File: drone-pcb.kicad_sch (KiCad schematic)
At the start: 46 parts, among them J1 Conn_01x02_Pin, J10 Conn_01x03_Pin, J11 Conn_01x03_Pin, J12 Conn_01x03_Pin, J2 Conn_01x02_Pin, J3 Conn_01x02_Pin, J4 Conn_01x02_Pin, J5 Conn_01x02_Pin, J6 Conn_01x02_Pin, J7 USB_C_Receptacle_USB2.0_16P, J8 Conn_01x02_Pin, J9 Conn_01x03_Pin, Q1 AO3400A, Q2 AO3400A, Q3 AO3400A, Q4 AO3400A, Q5 AO3400A, Q6 AO3400A, SW1 CK_KMS2xxGP, U1 STM32F030C8Tx, U2 nRF24L01P, U3 MCP73831-2-OT, U4 TLV75533PDBV

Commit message: test export after makefile genaralisation
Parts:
- added U5: MPU-6050, Sensor_Motion:InvenSense_QFN-24_4x4mm_P0.5mm, symbol Sensor_Motion:MPU-6050
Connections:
- net battery+ is gone; now on net Vmotor: J8.1 (Pin_1), U3.3 (V_{BAT}), U4.1 (IN), U4.3 (EN)
- net +3V3: now also U5.13 (VDD)
- net GND: now also U5.18 (GND)
- net m1: no longer R11.1
- net m2: no longer R12.1
- net m3: no longer R13.1
- net m4: no longer R14.1
- net m5: no longer R15.1
- net m6: no longer R16.1
- net at Q1.1 (G), R1.1: now also R11.1
- net at Q3.1 (G), R3.1: now also R13.1
- net at Q2.1 (G), R2.1: now also R12.1
- net at Q4.1 (G), R4.1: now also R14.1
- net at Q5.1 (G), R5.1: now also R15.1
- net at Q6.1 (G), R6.1: now also R16.1
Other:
- note added: "3.3V power rail buck from battery voltage"
- note removed: "3.3V power rail"

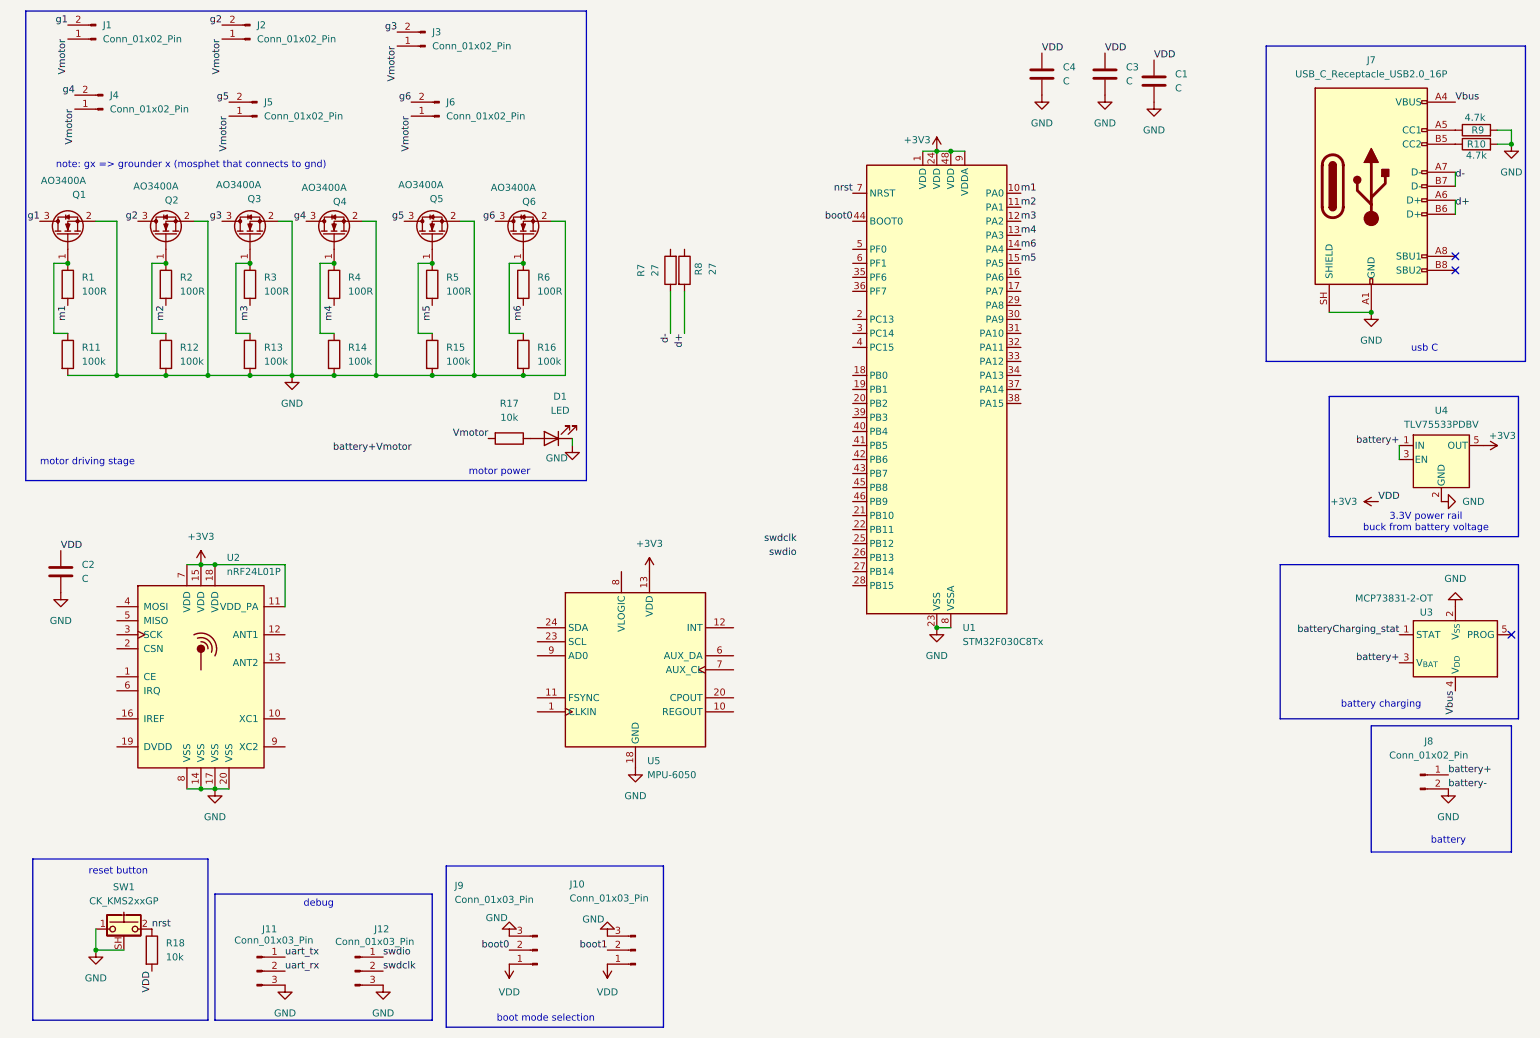
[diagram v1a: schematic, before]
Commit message: bypass the mcu gate driving series resistor for the pulldown in the motor driving mosfets
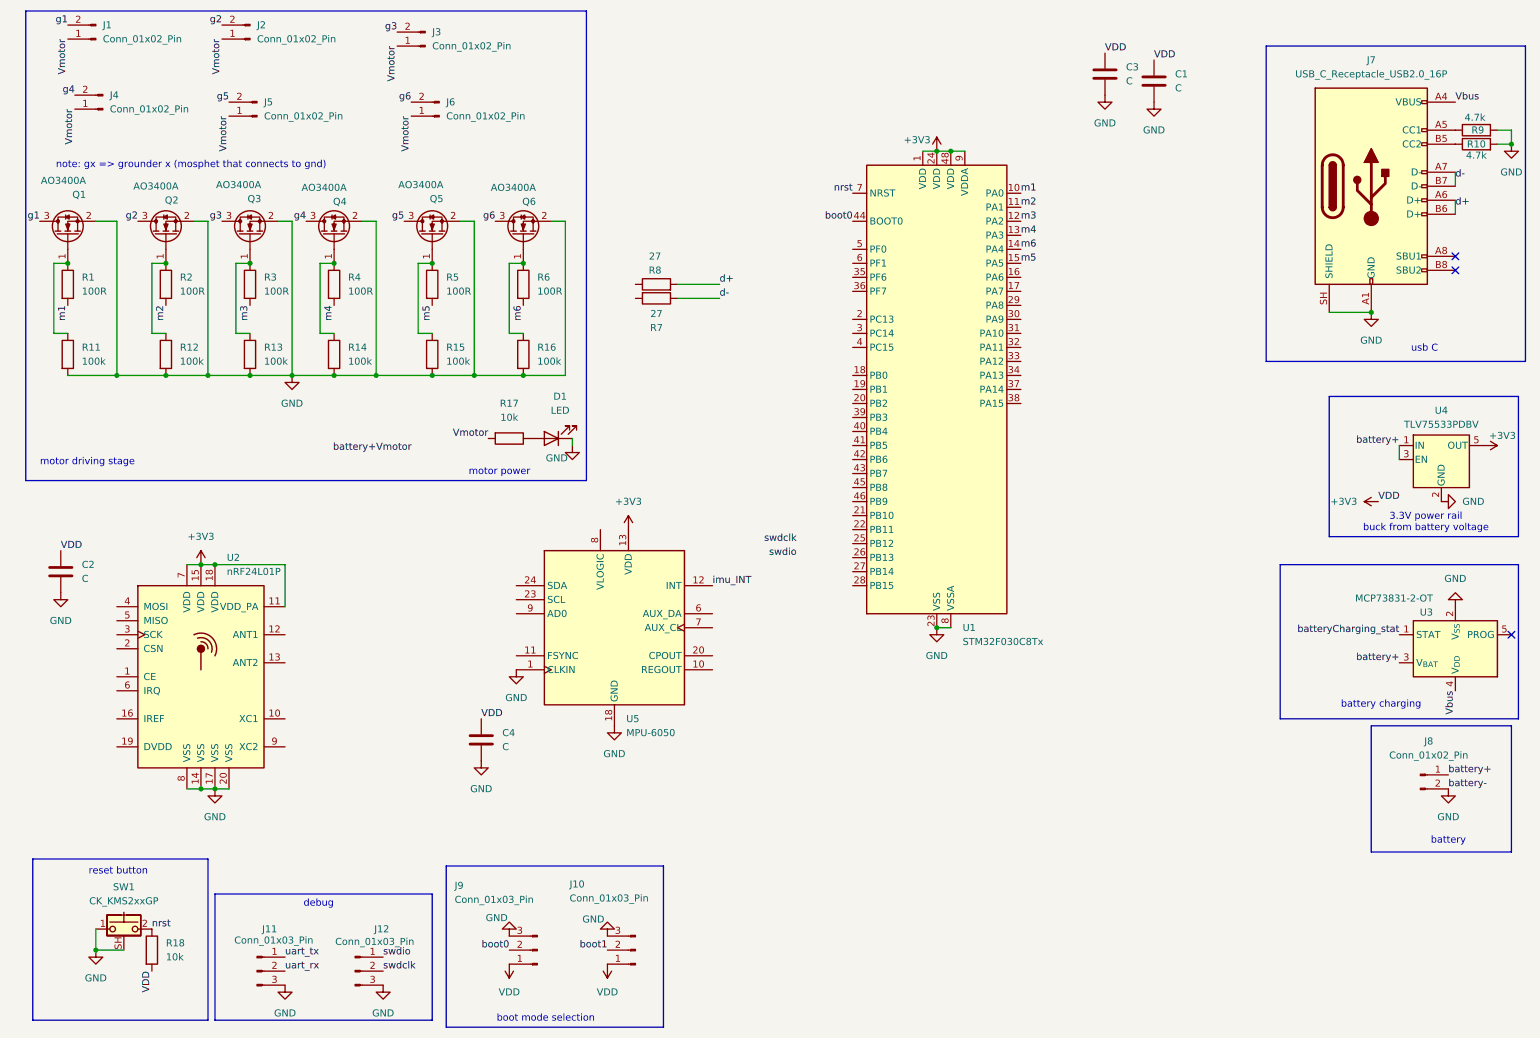
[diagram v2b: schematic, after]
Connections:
- net GND: now also U5.1 (CLKIN)
- net imu_INT: now reaches U5.12 (INT)
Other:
- moved on the sheet: C4, R7, R8, U5
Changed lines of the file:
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@@
 	(wire
 		(pts
-			(xy 132.08 63.5) (xy 132.08 71.12)
+			(xy 130.81 62.23) (xy 138.43 62.23)
 		)
 		(stroke
@@
 	(wire
 		(pts
-			(xy 129.54 63.5) (xy 129.54 71.12)
+			(xy 130.81 64.77) (xy 138.43 64.77)
 		)
 		(stroke
@@
 	)
 	(label "d-"
-		(at 129.54 71.12 270)
+		(at 138.43 64.77 0)
 		(effects
 			(font
 				(size 1.27 1.27)
 			)
-			(justify right bottom)
+			(justify left bottom)
 		)
 	)
@@
 	)
 	(label "VDD"
-		(at 196.85 20.32 0)
+		(at 95.25 140.97 0)
 		(effects
 			(font
@@
 		)
 	)
+	(label "imu_INT"
+		(at 137.16 116.84 0)
+		(effects
+			(font
+				(size 1.27 1.27)
+			)
+			(justify left bottom)
+		)
+	)
 	(label "m6"
 		(at 193.04 55.88 0)
@@
 	)
 	(label "d+"
-		(at 132.08 71.12 270)
+		(at 138.43 62.23 0)
 		(effects
 			(font
 				(size 1.27 1.27)
 			)
-			(justify right bottom)
+			(justify left bottom)
 		)
 	)
@@
 	(symbol
 		(lib_id "Sensor_Motion:MPU-6050")
-		(at 123.19 132.08 0)
+		(at 119.38 124.46 0)
 		(unit 1)
 		(body_style 1)
@@
 		(fields_autoplaced yes)
 		(property "Reference" "U5"
-			(at 125.3333 148.59 0)
+			(at 121.5233 140.97 0)
 			(show_name no)
 			(do_not_autoplace no)
@@
 		)
 		(property "Value" "MPU-6050"
-			(at 125.3333 151.13 0)
+			(at 121.5233 143.51 0)
 			(show_name no)
 			(do_not_autoplace no)
@@
 		)
 		(property "Footprint" "Sensor_Motion:InvenSense_QFN-24_4x4mm_P0.5mm"
-			(at 123.19 152.4 0)
+			(at 119.38 144.78 0)
 			(hide yes)
 			(show_name no)
@@
 		)
 		(property "Datasheet" "https://invensense.tdk.com/wp-content/uploads/2015/02/MPU-6000-Datasheet1.pdf"
-			(at 123.19 135.89 0)
+			(at 119.38 128.27 0)
 			(hide yes)
 			(show_name no)
@@
 		)
 		(property "Description" "InvenSense 6-Axis Motion Sensor, Gyroscope, Accelerometer, I2C"
-			(at 123.19 132.08 0)
+			(at 119.38 124.46 0)
 			(hide yes)
 			(show_name no)
@@
 	(symbol
 		(lib_id "power:GND")
-		(at 196.85 27.94 0)
+		(at 95.25 148.59 0)
 		(unit 1)
 		(body_style 1)
@@
 		(fields_autoplaced yes)
 		(property "Reference" "#PWR018"
-			(at 196.85 34.29 0)
+			(at 95.25 154.94 0)
 			(hide yes)
 			(show_name no)
@@
 		)
 		(property "Value" "GND"
-			(at 196.85 33.02 0)
+			(at 95.25 153.67 0)
 			(show_name no)
 			(do_not_autoplace no)
@@
 		)
 		(property "Footprint" ""
-			(at 196.85 27.94 0)
+			(at 95.25 148.59 0)
 			(hide yes)
 			(show_name no)
@@
 		)
 		(property "Datasheet" ""
-			(at 196.85 27.94 0)
+			(at 95.25 148.59 0)
 			(hide yes)
 			(show_name no)
@@
 		)
 		(property "Description" "Power symbol creates a global label with name \"GND\" , ground"
-			(at 196.85 27.94 0)
+			(at 95.25 148.59 0)
 			(hide yes)
 			(show_name no)
@@
 	(symbol
 		(lib_id "Device:R")
-		(at 129.54 59.69 180)
+		(at 127 64.77 270)
 		(unit 1)
 		(body_style 1)
@@
 		(dnp no)
 		(property "Reference" "R7"
-			(at 124.206 59.69 90)
+			(at 127 70.104 90)
 			(show_name no)
 			(do_not_autoplace no)
@@
 		)
 		(property "Value" "27"
-			(at 126.746 59.69 90)
+			(at 127 67.564 90)
 			(show_name no)
 			(do_not_autoplace no)
@@
 		)
 		(property "Footprint" "Resistor_SMD:R_0805_2012Metric_Pad1.20x1.40mm_HandSolder"
-			(at 131.318 59.69 90)
+			(at 127 62.992 90)
 			(hide yes)
 			(show_name no)
@@
 		)
 		(property "Datasheet" ""
-			(at 129.54 59.69 0)
+			(at 127 64.77 0)
 			(hide yes)
 			(show_name no)
@@
 		)
 		(property "Description" "Resistor"
-			(at 129.54 59.69 0)
+			(at 127 64.77 0)
 			(hide yes)
 			(show_name no)
@@
 	(symbol
 		(lib_id "Device:C")
-		(at 196.85 24.13 0)
+		(at 95.25 144.78 0)
 		(unit 1)
 		(body_style 1)
@@
 		(fields_autoplaced yes)
 		(property "Reference" "C4"
-			(at 200.66 22.8599 0)
+			(at 99.06 143.5099 0)
 			(show_name no)
 			(do_not_autoplace no)
@@
 		)
 		(property "Value" "C"
-			(at 200.66 25.3999 0)
+			(at 99.06 146.0499 0)
 			(show_name no)
 			(do_not_autoplace no)
@@
 		)
 		(property "Footprint" "Capacitor_SMD:C_0805_2012Metric_Pad1.18x1.45mm_HandSolder"
-			(at 197.8152 27.94 0)
+			(at 96.2152 148.59 0)
 			(hide yes)
 			(show_name no)
@@
 		)
 		(property "Datasheet" ""
-			(at 196.85 24.13 0)
+			(at 95.25 144.78 0)
 			(hide yes)
 			(show_name no)
@@
 		)
 		(property "Description" "Unpolarized capacitor"
-			(at 196.85 24.13 0)
+			(at 95.25 144.78 0)
 			(hide yes)
 			(show_name no)
@@
 	(symbol
 		(lib_id "power:GND")
-		(at 123.19 149.86 0)
+		(at 119.38 142.24 0)
 		(unit 1)
 		(body_style 1)
@@
 		(fields_autoplaced yes)
 		(property "Reference" "#PWR024"
-			(at 123.19 156.21 0)
+			(at 119.38 148.59 0)
 			(hide yes)
 			(show_name no)
@@
 		)
 		(property "Value" "GND"
-			(at 123.19 154.94 0)
+			(at 119.38 147.32 0)
 			(show_name no)
 			(do_not_autoplace no)
@@
 		)
 		(property "Footprint" ""
-			(at 123.19 149.86 0)
+			(at 119.38 142.24 0)
 			(hide yes)
 			(show_name no)
@@
 		)
 		(property "Datasheet" ""
-			(at 123.19 149.86 0)
+			(at 119.38 142.24 0)
 			(hide yes)
 			(show_name no)
@@
 		)
 		(property "Description" "Power symbol creates a global label with name \"GND\" , ground"
-			(at 123.19 149.86 0)
+			(at 119.38 142.24 0)
 			(hide yes)
 			(show_name no)
@@
 	(symbol
 		(lib_id "power:+3V3")
-		(at 125.73 114.3 0)
+		(at 121.92 106.68 0)
 		(unit 1)
 		(body_style 1)
@@
 		(fields_autoplaced yes)
 		(property "Reference" "#PWR025"
-			(at 125.73 118.11 0)
+			(at 121.92 110.49 0)
 			(hide yes)
 			(show_name no)
@@
 		)
 		(property "Value" "+3V3"
-			(at 125.73 109.22 0)
+			(at 121.92 101.6 0)
 			(show_name no)
 			(do_not_autoplace no)
@@
 		)
 		(property "Footprint" ""
-			(at 125.73 114.3 0)
+			(at 121.92 106.68 0)
 			(hide yes)
 			(show_name no)
@@
 		)
 		(property "Datasheet" ""
-			(at 125.73 114.3 0)
+			(at 121.92 106.68 0)
 			(hide yes)
 			(show_name no)
@@
 		)
 		(property "Description" "Power symbol creates a global label with name \"+3V3\""
-			(at 125.73 114.3 0)
+			(at 121.92 106.68 0)
 			(hide yes)
 			(show_name no)
@@
 	)
 	(symbol
+		(lib_id "power:GND")
+		(at 101.6 132.08 0)
+		(unit 1)
+		(body_style 1)
+		(exclude_from_sim no)
+		(in_bom yes)
+		(on_board yes)
+		(in_pos_files yes)
+		(dnp no)
+		(fields_autoplaced yes)
+		(property "Reference" "#PWR027"
+			(at 101.6 138.43 0)
+			(hide yes)
+			(show_name no)
+			(do_not_autoplace no)
+			(effects
+				(font
+					(size 1.27 1.27)
+				)
+			)
+		)
+		(property "Value" "GND"
+			(at 101.6 137.16 0)
+			(show_name no)
+			(do_not_autoplace no)
+			(effects
+				(font
+					(size 1.27 1.27)
+				)
+			)
+		)
+		(property "Footprint" ""
+			(at 101.6 132.08 0)
+			(hide yes)
+			(show_name no)
+			(do_not_autoplace no)
+			(effects
+				(font
+					(size 1.27 1.27)
+				)
+			)
+		)
+		(property "Datasheet" ""
+			(at 101.6 132.08 0)
+			(hide yes)
+			(show_name no)
+			(do_not_autoplace no)
+			(effects
+				(font
+					(size 1.27 1.27)
+				)
+			)
+		)
+		(property "Description" "Power symbol creates a global label with name \"GND\" , ground"
+			(at 101.6 132.08 0)
+			(hide yes)
+			(show_name no)
+			(do_not_autoplace no)
+			(effects
+				(font
+					(size 1.27 1.27)
+				)
+			)
+		)
+		(pin "1"
+		)
+		(instances
+			(project "drone-pcb"
+				(path "/6424a1a8-ac3c-40bd-aa54-81cdf86a6261"
+					(reference "#PWR027")
+					(unit 1)
+				)
+			)
+		)
+	)
+	(symbol
 		(lib_name "R_1")
 		(lib_id "Device:R")
@@
 	(symbol
 		(lib_id "Device:R")
-		(at 132.08 59.69 0)
+		(at 127 62.23 90)
 		(unit 1)
 		(body_style 1)
@@
 		(dnp no)
 		(property "Reference" "R8"
-			(at 134.62 59.436 90)
+			(at 126.746 59.69 90)
 			(show_name no)
 			(do_not_autoplace no)
@@
 		)
 		(property "Value" "27"
-			(at 137.16 59.436 90)
+			(at 126.746 57.15 90)
 			(show_name no)
 			(do_not_autoplace no)
@@
 		)
 		(property "Footprint" "Resistor_SMD:R_0805_2012Metric_Pad1.20x1.40mm_HandSolder"
-			(at 130.302 59.69 90)
+			(at 127 64.008 90)
 			(hide yes)
 			(show_name no)
@@
 		)
 		(property "Datasheet" ""
-			(at 132.08 59.69 0)
+			(at 127 62.23 0)
 			(hide yes)
 			(show_name no)
@@
 		)
 		(property "Description" "Resistor"
-			(at 132.08 59.69 0)
+			(at 127 62.23 0)
 			(hide yes)
 			(show_name no)

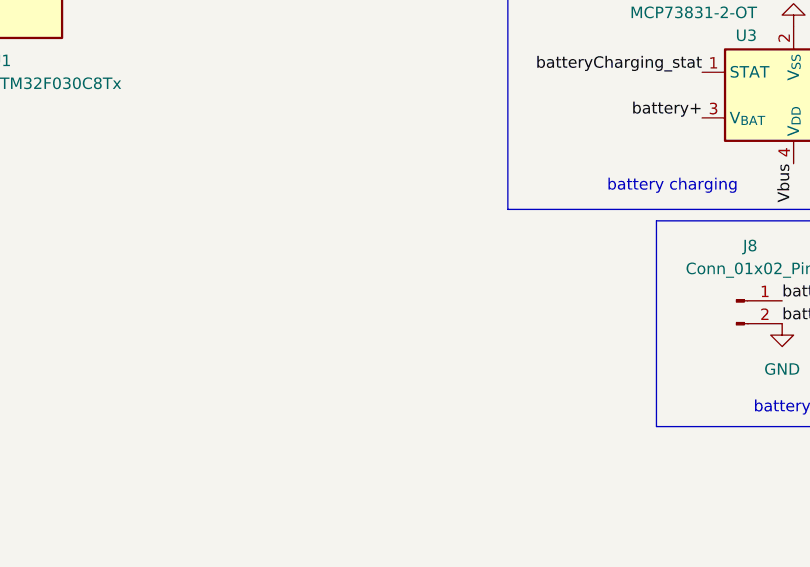
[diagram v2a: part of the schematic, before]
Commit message: add dw01a battery protector
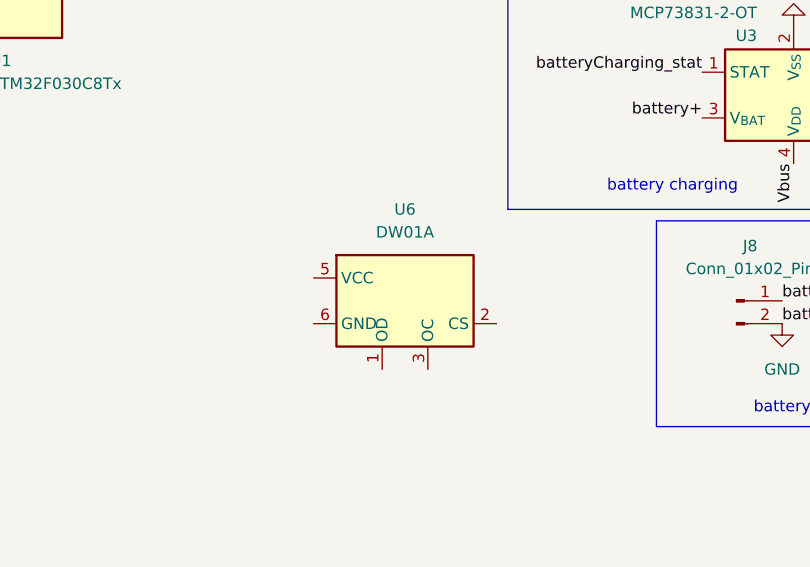
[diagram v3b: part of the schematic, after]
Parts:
- added U6: DW01A, Package_TO_SOT_SMD:SOT-23-6, symbol Battery_Management:DW01A
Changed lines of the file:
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@@
+	)
+	(symbol
+		(lib_id "Battery_Management:DW01A")
+		(at 228.6 151.13 0)
+		(unit 1)
+		(body_style 1)
+		(exclude_from_sim no)
+		(in_bom yes)
+		(on_board yes)
+		(in_pos_files yes)
+		(dnp no)
+		(fields_autoplaced yes)
+		(property "Reference" "U6"
+			(at 228.6 140.97 0)
+			(show_name no)
+			(do_not_autoplace no)
+			(effects
+				(font
+					(size 1.27 1.27)
+				)
+			)
+		)
+		(property "Value" "DW01A"
+			(at 228.6 143.51 0)
+			(show_name no)
+			(do_not_autoplace no)
+			(effects
+				(font
+					(size 1.27 1.27)
+				)
+			)
+		)
+		(property "Footprint" "Package_TO_SOT_SMD:SOT-23-6"
+			(at 228.6 151.13 0)
+			(hide yes)
+			(show_name no)
+			(do_not_autoplace no)
+			(effects
+				(font
+					(size 1.27 1.27)
+				)
+			)
+		)
+		(property "Datasheet" "https://hmsemi.com/downfile/DW01A.PDF"
+			(at 228.6 151.13 0)
+			(hide yes)
+			(show_name no)
+			(do_not_autoplace no)
+			(effects
+				(font
+					(size 1.27 1.27)
+				)
+			)
+		)
+		(property "Description" "Overcharge, overcurrent and overdischarge protection IC for single cell lithium-ion/polymer battery"
+			(at 228.854 149.606 0)
+			(hide yes)
+			(show_name no)
+			(do_not_autoplace no)
+			(effects
+				(font
+					(size 1.27 1.27)
+				)
+			)
+		)
+		(pin "6"
+		)
+		(pin "4"
+		)
+		(pin "5"
+		)
+		(pin "3"
+		)
+		(pin "1"
+		)
+		(pin "2"
+		)
+		(instances
+			(project "drone-pcb"
+				(path "/6424a1a8-ac3c-40bd-aa54-81cdf86a6261"
+					(reference "U6")
+					(unit 1)
+				)
+			)
+		)
 	)
 	(symbol

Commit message: change to stm32f108
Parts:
- removed U1: STM32F030C8Tx, Package_QFP:LQFP-48_7x7mm_P0.5mm, symbol MCU_ST_STM32F0:STM32F030C8Tx
- added U1: STM32F103C8Tx, Package_QFP:LQFP-48_7x7mm_P0.5mm, symbol MCU_ST_STM32F1:STM32F103C8Tx
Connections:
- net +3V3: now also U1.1 (VBAT), U1.24 (VDD), U1.36 (VDD), U1.48 (VDD), U1.9 (VDDA)
- net GND: now also U1.23 (VSS), U1.35 (VSS), U1.47 (VSS), U1.8 (VSSA)
- net boot0: now also U1.44 (BOOT0)
- net nrst: now also U1.7 (NRST)

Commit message: half done
placed chips, not routed, schematic incomplete
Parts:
- removed C4: C, Capacitor_SMD:C_0805_2012Metric_Pad1.18x1.45mm_HandSolder, symbol Device:C
- removed J5, J6: Conn_01x02_Pin, Connector_JST:JST_XH_S2B-XH-A-1_1x02_P2.50mm_Horizontal, symbol Connector:Conn_01x02_Pin
- removed R16: 100k, Resistor_SMD:R_0805_2012Metric_Pad1.20x1.40mm_HandSolder, symbol Device:R
- removed R5, R6: 100R, Resistor_SMD:R_0805_2012Metric_Pad1.20x1.40mm_HandSolder, symbol Device:R
- removed R7, R8: 27, Resistor_SMD:R_0805_2012Metric_Pad1.20x1.40mm_HandSolder, symbol Device:R
- removed SW1: CK_KMS2xxGP, Button_Switch_SMD:SW_SPST_CK_KMS2xxGP, symbol Switch:CK_KMS2xxGP
- removed U5: MPU-6050, Sensor_Motion:InvenSense_QFN-24_4x4mm_P0.5mm, symbol Sensor_Motion:MPU-6050
- added D2: LED, LED_SMD:LED_0805_2012Metric_Pad1.15x1.40mm_HandSolder, symbol Device:LED
- added SW2: SW_Push_Dual_x2, ch32-devBoard-symbols:smd-push-button-TS3425PA, symbol Switch:SW_Push_Dual_x2
- added U3: MPU-9250, Sensor_Motion:InvenSense_QFN-24_3x3mm_P0.4mm, symbol Sensor_Motion:MPU-9250
- added Y1: Crystal, symbol Device:Crystal
- R1: renamed from R9; value 4.7k -> 5.1k
- R15: value 100k -> 10k
- R2: renamed from R10; value 4.7k -> 5.1k
- renumbered C3 to C1, C1 to C2, C2 to C3, J12 to J10, J4 to J3, J3 to J4, J7 to J5, J8 to J6, J9 to J7, J10 to J8, J11 to J9, R12 to R10, R13 to R11, R14 to R12, R17 to R13, R18 to R14, R1 to R3, R2 to R4, R3 to R5, R4 to R6, R11 to R9, U4 to U2, U3 to U4, U2 to U5
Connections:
- net +3V3: now also U6.5 (VCC), U3.13 (VDD)
- net GND: now also U6.6 (GND), D2.1 (K), SW2.1 (C), U3.18 (GND); no longer Q5.2 (S), Q6.2 (S), R15.2
- net boot1: now also U1.20 (PB2)
- net d+: now also U1.33 (PA12)
- net d-: now also U1.32 (PA11)
- net m1: now also U1.10 (PA0)
- net m2: now also U1.11 (PA1)
- net m3: now also U1.12 (PA2)
- net m4: now also U1.13 (PA3)
- net nrst: now also SW2.2 (D)
- net swdclk: now also U1.37 (PA14)
- net swdio: now also U1.34 (PA13)
- net at R15.1: now also D2.2 (A); no longer Q5.1 (G)
- net discharge_gate: now reaches Q6.1 (G)
- net discharge_gate: now also U6.1 (OD)
- net led: now reaches U1.18 (PB0)
- net led: now also R15.2
- net charge_gate: now reaches U6.3 (OC)
- net charge_gate: now also Q5.1 (G)
- net Vmotor renamed Vbat
- net Vbat: now also Q6.2 (S); no longer J6.1 (Pin_1), U4.3 (V_{BAT})
- net g5: no longer names the net of Q5.3 (D)
- net g5: now also U4.3 (V_{BAT})
- net g6 renamed battery+
- net battery+: now also J6.1 (Pin_1), Q5.2 (S)
- new net imu_fsync: U3.11 (FSYNC)
- new net imu_int: U3.12 (INT)
- new net imu_miso: U3.9 (AD0/MISO)
- new net imu_mosi: U3.24 (SDA/MOSI)
- new net imu_spi_clk: U3.23 (SCL/SCLK)
- new net imu_spi_cs: U3.22 (~{CS})
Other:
- note added: "battery power supply"
- note added: "indicator led"
- note added: "protection"
- note removed: "battery"
- note removed: "motor power"
- moved on the sheet: D1, J4, J6, R13, U2, U6
